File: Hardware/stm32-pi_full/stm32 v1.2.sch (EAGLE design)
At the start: 286 parts, among them IC2 AD8519KS, J1 JUMPER-SMT_2_NC_TRACE_NO-SILK, Q1 PNP, Q2 NPN, Q3 NPN, U1 ESP32-WROOM-32D

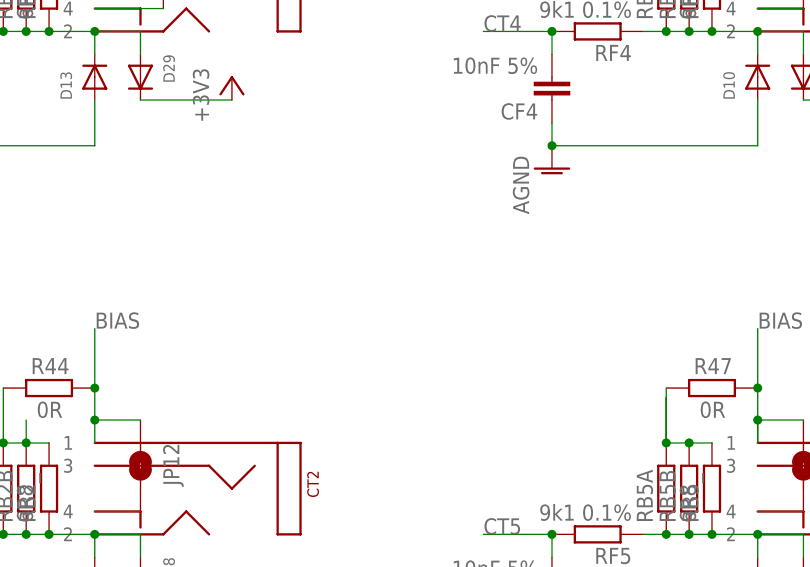
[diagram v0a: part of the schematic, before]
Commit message: pulse detect fix. separated readings timer and posting timer implemented.
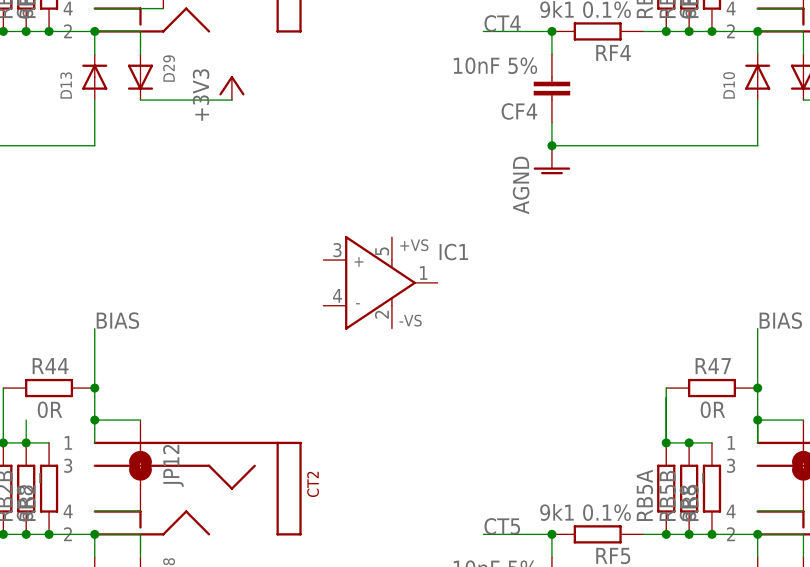
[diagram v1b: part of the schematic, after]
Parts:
- added IC1: AD8519KS, analog-devices:AD8519KS
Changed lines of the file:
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@@
 <part name="C55" library="rcl" library_urn="urn:adsk.eagle:library:334" deviceset="C-EU" device="C0805" package3d_urn="urn:adsk.eagle:package:23617/2" value="47uF"/>
 <part name="TP12" library="SparkFun-Connectors" deviceset="TEST-POINT" device="3"/>
+<part name="IC1" library="analog-devices" library_urn="urn:adsk.eagle:library:102" deviceset="AD8519" device="KS" package3d_urn="urn:adsk.eagle:package:3966/1" value=""/>
 </parts>
 <sheets>
@@
 <attribute name="NAME" x="-2.794" y="68.58" size="1.778" layer="95" font="vector" rot="R90"/>
 </instance>
+<instance part="IC1" gate="P" x="271.78" y="152.4" smashed="yes">
+<attribute name="NAME" x="279.4" y="154.94" size="1.778" layer="95"/>
+<attribute name="VALUE" x="279.4" y="148.59" size="1.778" layer="96"/>
+</instance>
 </instances>

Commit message: modified:   Hardware/stm32-pi_full/stm32 v1.2.brd 	modified:   Hardware/stm32-pi_full/stm32 v1.2.sch 	modified:   Software/Sombrero_VE_Working6/build/Sombrero_VE_Working6.bin
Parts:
- removed C20: 2.2nF, rcl:C-EUC0603
- removed C35, C36: (no value), rcl:C-EUC0603
- removed C50: 1uF, rcl:C-EUC0603
- removed D10, D11, D12, D13, D15, D16, D19, D20, D24, D25, D27, D28, D29, D5, D6, D7, D8, D9: ESD5Z3.3T1G, microbuilder:DIODESOD-523
- removed IC1, IC2: AD8519KS, analog-devices:AD8519KS
- removed JP11, JP13, JP15: JUMPER-SMT_2_NO_NO-SILK_ROUND, SparkFun-Jumpers:JUMPER-SMT_2_NO_NO-SILK_ROUND
- removed R23: 1k, resistor:R-EU_R0603
- removed R38: 39k, resistor:R-EU_R0603
- removed R46, R47, R48: 0R, rcl:R-EU_R0603
- removed R54: 10k, resistor:R-EU_R0603
- removed R6: 0R, resistor:R-EU_R0603
- removed RB1B, RB2B, RB3B, RB4B, RB5B, RB6B, RB7B, RB8B, RB9B: (no value), rcl:R-EU_R0805
- removed TP3, TP5, TP6: TEST-POINTPOGO_PTH, SparkFun-Connectors:TEST-POINTPOGO_PTH
- added LMV1, LMV2, LMV3: LMV824IDG4, LMV824IDG4:LMV824IDG4
- added RB11, RB12, RB13: 510R, rcl:R-EU_R0805
- added RB44, RB55, RB66: 680R, rcl:R-EU_R0805
- added SJ1: JUMPER-SMT_2_NC_TRACE_NO-SILK, SparkFun-Jumpers:JUMPER-SMT_2_NC_TRACE_NO-SILK
- added U2: RFM69HCW/RFM95W, microbuilder:RFM69HCW_SMT
- R55: value 91k -> 10k
- renumbered RB1A to RB1, RB2A to RB2, RB3A to RB3, RB4A to RB4, RB5A to RB5, RB6A to RB6, RB7A to RB7, RB8A to RB8, RB9A to RB9
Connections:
- net CT4 renamed CT4_ADC
- net CT5 renamed CT5_ADC
- net CT6 renamed CT6_ADC
- removed net N$25: R46.2, RB6.2, RB6B.2, RB6_.2
- new net BIAS1: D2.A, D3.C
- new net BIAS456: LMV2.1IN+, LMV2.2IN+, LMV2.3IN+, LMV2.4IN-, LMV2.4OUT, RB44.2, RB55.2, RB66.2
- new net CT4_OUT: LMV2.1OUT, RB11.1, RF4.1
- new net CT5_OUT: LMV2.2OUT, RB12.1, RF5.1
- new net CT6_OUT: LMV2.3OUT, RB13.2, RF6.1
- new net N$12: CT5.3
- new net N$38: CT4.3
- new net N$40: CT6.1, RB6.2, RB66.1, RB6_.2
- net +3V3ANA: now also LMV1.VCC+, LMV2.VCC+, LMV3.VCC+; no longer D15.C, D16.C, D19.C, D20.C, D24.C, D25.C, D27.C, D28.C, D29.C, IC2.+VS
- net AGND: now also LMV1.GND/VCC-, LMV2.GND/VCC-, LMV3.GND/VCC-; no longer C35.2, C36.2, C50.2, D10.A, D11.A, D12.A, D13.A, D5.A, D6.A, D7.A, D8.A, D9.A, IC2.-VS, R54.2
- net BIAS: now also LMV2.4IN+; no longer C35.1, C36.1, CT4.1, CT5.1, CT6.1, D2.A, D3.C, JP11.1, JP13.1, JP15.1, R23.2, R38.1, R46.1, R47.1, R48.1, R6.2, TP3.1
- net CT_IN1: no longer D13.C, D29.A, RB1B.1
- net CT_IN2: no longer D12.C, D28.A, RB2B.1
- net CT_IN3: no longer D11.C, D27.A, RB3B.1
- net CT_IN4: now also LMV2.1IN-, RB11.2; no longer D10.C, D25.A, RB4B.1, RF4.1
- net CT_IN5: now also LMV2.2IN-, RB12.2; no longer D20.A, D9.C, RB5B.1, RF5.1
- net CT_IN6: now also LMV2.3IN-, RB13.1; no longer D24.A, D8.C, RB6B.1, RF6.1
- net CT_IN7: no longer D19.A, D7.C, RB7B.1
- net CT_IN8: no longer D16.A, D6.C, RB8B.1
- net CT_IN9: no longer D15.A, D5.C, RB9B.1
- net N$10: no longer JP13.2
- net N$2: no longer JP11.2
- net N$20: no longer JP15.2
- net N$24: now also CT6.3; no longer R47.2, RB5.2, RB5B.2, RB5_.2
- net N$26: no longer RB1B.2
- net N$27: no longer RB2B.2
- net N$29: no longer RB8B.2
- net N$34: no longer RB9B.2
- net N$35: now also CT4.1, RB44.1; no longer R48.2, RB4B.2
- net N$36: no longer RB7B.2
- net N$37: no longer RB3B.2
- net N$7: now also CT5.1, RB5.2, RB55.1, RB5_.2; no longer C50.1, R23.1
- net OPAMP_INVERT-: now also SJ1.1; no longer C20.1, IC2.IN-, R38.2, R54.1, TP6.1
- net OPAMP_NON-INVERT+: no longer IC2.IN+, TP2.1
- net OPAMP_OUT: now also SJ1.2, TP2.1; no longer C20.2, IC2.OUT, R6.1, TP5.1
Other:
- note added: "RFMxx"
- note removed: "RFM69"
- moved on the sheet: CF4, CF5, CF6, CV1, CV2, CV3, CV4, D1, D2, D3, D4, LMV824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

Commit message: update
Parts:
- RB1, RB2, RB3, RB4, RB5, RB6, RB7, RB8, RB9: value 6R8 -> 6R81
- RB11, RB12, RB13: value 510R -> 510R 0.1%
- RB44, RB55, RB66: value 680R -> 680R | 681R 0.1%
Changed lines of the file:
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@@
 <drawing>
 <settings>
-<setting alwaysvectorfont="no"/>
+<setting alwaysvectorfont="yes"/>
 <setting keepoldvectorfont="yes"/>
 <setting verticaltext="up"/>
@@
 <part name="TP20" library="SparkFun-Connectors" deviceset="TEST-POINT" device="POGO_PTH" value="TEST-POINTPOGO_PTH"/>
 <part name="HSE" library="6mm 3m5mm crystal multicomp pro abracon" deviceset="6MM_3.5MM_CRYSTAL" device=""/>
-<part name="RB1" library="rcl" library_urn="urn:adsk.eagle:library:334" deviceset="R-EU_" device="R0805" package3d_urn="urn:adsk.eagle:package:23553/2" value="6R8"/>
-<part name="RB4" library="rcl" library_urn="urn:adsk.eagle:library:334" deviceset="R-EU_" device="R0805" package3d_urn="urn:adsk.eagle:package:23553/2" value="6R8"/>
-<part name="RB7" library="rcl" library_urn="urn:adsk.eagle:library:334" deviceset="R-EU_" device="R0805" package3d_urn="urn:adsk.eagle:package:23553/2" value="6R8"/>
-<part name="RB8" library="rcl" library_urn="urn:adsk.eagle:library:334" deviceset="R-EU_" device="R0805" package3d_urn="urn:adsk.eagle:package:23553/2" value="6R8"/>
-<part name="RB5" library="rcl" library_urn="urn:adsk.eagle:library:334" deviceset="R-EU_" device="R0805" package3d_urn="urn:adsk.eagle:package:23553/2" value="6R8"/>
-<part name="RB9" library="rcl" library_urn="urn:adsk.eagle:library:334" deviceset="R-EU_" device="R0805" package3d_urn="urn:adsk.eagle:package:23553/2" value="6R8"/>
-<part name="RB6" library="rcl" library_urn="urn:adsk.eagle:library:334" deviceset="R-EU_" device="R0805" package3d_urn="urn:adsk.eagle:package:23553/2" value="6R8"/>
-<part name="RB2" library="rcl" library_urn="urn:adsk.eagle:library:334" deviceset="R-EU_" device="R0805" package3d_urn="urn:adsk.eagle:package:23553/2" value="6R8"/>
-<part name="RB3" library="rcl" library_urn="urn:adsk.eagle:library:334" deviceset="R-EU_" device="R0805" package3d_urn="urn:adsk.eagle:package:23553/2" value="6R8"/>
+<part name="RB1" library="rcl" library_urn="urn:adsk.eagle:library:334" deviceset="R-EU_" device="R0805" package3d_urn="urn:adsk.eagle:package:23553/2" value="6R81"/>
+<part name="RB4" library="rcl" library_urn="urn:adsk.eagle:library:334" deviceset="R-EU_" device="R0805" package3d_urn="urn:adsk.eagle:package:23553/2" value="6R81"/>
+<part name="RB7" library="rcl" library_urn="urn:adsk.eagle:library:334" deviceset="R-EU_" device="R0805" package3d_urn="urn:adsk.eagle:package:23553/2" value="6R81"/>
+<part name="RB8" library="rcl" library_urn="urn:adsk.eagle:library:334" deviceset="R-EU_" device="R0805" package3d_urn="urn:adsk.eagle:package:23553/2" value="6R81"/>
+<part name="RB5" library="rcl" library_urn="urn:adsk.eagle:library:334" deviceset="R-EU_" device="R0805" package3d_urn="urn:adsk.eagle:package:23553/2" value="6R81"/>
+<part name="RB9" library="rcl" library_urn="urn:adsk.eagle:library:334" deviceset="R-EU_" device="R0805" package3d_urn="urn:adsk.eagle:package:23553/2" value="6R81"/>
+<part name="RB6" library="rcl" library_urn="urn:adsk.eagle:library:334" deviceset="R-EU_" device="R0805" package3d_urn="urn:adsk.eagle:package:23553/2" value="6R81"/>
+<part name="RB2" library="rcl" library_urn="urn:adsk.eagle:library:334" deviceset="R-EU_" device="R0805" package3d_urn="urn:adsk.eagle:package:23553/2" value="6R81"/>
+<part name="RB3" library="rcl" library_urn="urn:adsk.eagle:library:334" deviceset="R-EU_" device="R0805" package3d_urn="urn:adsk.eagle:package:23553/2" value="6R81"/>
 <part name="R33" library="rcl" library_urn="urn:adsk.eagle:library:334" deviceset="R-EU_" device="R0603" package3d_urn="urn:adsk.eagle:package:23555/3" value="10k"/>
 <part name="+3V19" library="supply1" library_urn="urn:adsk.eagle:library:371" deviceset="+3V3" device=""/>
@@
 <attribute name="MPN" value="MBR130LSFT1G"/>
 </part>
-<part name="RB55" library="rcl" library_urn="urn:adsk.eagle:library:334" deviceset="R-EU_" device="R0805" package3d_urn="urn:adsk.eagle:package:23553/2" value="680R"/>
+<part name="RB55" library="rcl" library_urn="urn:adsk.eagle:library:334" deviceset="R-EU_" device="R0805" package3d_urn="urn:adsk.eagle:package:23553/2" value="680R | 681R 0.1%"/>
 <part name="U2" library="microbuilder" deviceset="RFM69HCW" device="_SMT" value="RFM69HCW/RFM95W"/>
-<part name="RB11" library="rcl" library_urn="urn:adsk.eagle:library:334" deviceset="R-EU_" device="R0805" package3d_urn="urn:adsk.eagle:package:23553/2" value="510R"/>
-<part name="RB44" library="rcl" library_urn="urn:adsk.eagle:library:334" deviceset="R-EU_" device="R0805" package3d_urn="urn:adsk.eagle:package:23553/2" value="680R"/>
-<part name="RB66" library="rcl" library_urn="urn:adsk.eagle:library:334" deviceset="R-EU_" device="R0805" package3d_urn="urn:adsk.eagle:package:23553/2" value="680R"/>
+<part name="RB11" library="rcl" library_urn="urn:adsk.eagle:library:334" deviceset="R-EU_" device="R0805" package3d_urn="urn:adsk.eagle:package:23553/2" value="510R 0.1%"/>
+<part name="RB44" library="rcl" library_urn="urn:adsk.eagle:library:334" deviceset="R-EU_" device="R0805" package3d_urn="urn:adsk.eagle:package:23553/2" value="680R | 681R 0.1%"/>
+<part name="RB66" library="rcl" library_urn="urn:adsk.eagle:library:334" deviceset="R-EU_" device="R0805" package3d_urn="urn:adsk.eagle:package:23553/2" value="680R | 681R 0.1%"/>
 <part name="LMV1" library="LMV824IDG4" deviceset="LMV824IDG4" device=""/>
 <part name="LMV2" library="LMV824IDG4" deviceset="LMV824IDG4" device=""/>
 <part name="LMV3" library="LMV824IDG4" deviceset="LMV824IDG4" device=""/>
-<part name="RB12" library="rcl" library_urn="urn:adsk.eagle:library:334" deviceset="R-EU_" device="R0805" package3d_urn="urn:adsk.eagle:package:23553/2" value="510R"/>
-<part name="RB13" library="rcl" library_urn="urn:adsk.eagle:library:334" deviceset="R-EU_" device="R0805" package3d_urn="urn:adsk.eagle:package:23553/2" value="510R"/>
+<part name="RB12" library="rcl" library_urn="urn:adsk.eagle:library:334" deviceset="R-EU_" device="R0805" package3d_urn="urn:adsk.eagle:package:23553/2" value="510R 0.1%"/>
+<part name="RB13" library="rcl" library_urn="urn:adsk.eagle:library:334" deviceset="R-EU_" device="R0805" package3d_urn="urn:adsk.eagle:package:23553/2" value="510R 0.1%"/>
 </parts>
 <sheets>

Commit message: brd changes
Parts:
- removed JP10, JP12, JP14, JP16, JP17, JP18: JUMPER-SMT_2_NO_NO-SILK_ROUND, SparkFun-Jumpers:JUMPER-SMT_2_NO_NO-SILK_ROUND
- removed R42, R44, R45, R49, R50, R51: 0R, rcl:R-EU_R0603
- added RB10, RB14, RB15, RB16, RB17, RB18: 510R 0.1%, rcl:R-EU_R0805
- added RB19, RB20, RB21, RB22, RB23, RB24: 680R | 681R 0.1%, rcl:R-EU_R0805
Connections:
- net CT1 renamed CT1_ADC
- net CT2 renamed CT2_ADC
- net CT3 renamed CT3_ADC
- removed net N$29: R50.2, RB8.2, RB8_.2
- removed net N$34: R51.2, RB9.2, RB9_.2
- removed net N$37: R45.2, RB3.2, RB3_.2
- new net BIAS123: LMV1.1IN+, LMV1.2IN+, LMV1.3IN+, LMV1.4IN-, LMV1.4OUT, RB19.2, RB20.2, RB21.2
- new net BIAS789: LMV3.1IN+, LMV3.2IN+, LMV3.3IN+, LMV3.4IN-, LMV3.4OUT, RB22.2, RB23.2, RB24.2
- new net CT1_OUT: LMV1.1OUT, RB10.1, RF1.1
- new net CT2_OUT: LMV1.2OUT, RB14.1, RF2.1
- new net CT3_OUT: LMV1.3OUT, RB15.2, RF3.1
- new net CT7_OUT: LMV3.1OUT, RB16.1, RF7.1
- new net CT8_OUT: LMV3.2OUT, RB17.1, RF8.1
- new net CT9_OUT: LMV3.3OUT, RB18.2, RF9.1
- new net N$43: CT9.1, RB24.1, RB9.2, RB9_.2
- new net N$45: CT8.1, RB23.1, RB8.2, RB8_.2
- new net N$46: CT7.1, RB22.1, RB7.2, RB7_.2
- net BIAS: now also LMV1.4IN+, LMV3.4IN+; no longer CT1.1, CT2.1, CT3.1, CT7.1, CT8.1, CT9.1, JP10.1, JP12.1, JP14.1, JP16.1, JP17.1, JP18.1, R42.1, R44.1, R45.1, R49.1, R50.1, R51.1
- net CT_IN1: now also LMV1.1IN-, RB10.2; no longer RF1.1
- net CT_IN2: now also LMV1.2IN-, RB14.2; no longer RF2.1
- net CT_IN3: now also LMV1.3IN-, RB15.1; no longer RF3.1
- net CT_IN7: now also LMV3.1IN-, RB16.2; no longer RF7.1
- net CT_IN8: now also LMV3.2IN-, RB17.2; no longer RF8.1
- net CT_IN9: now also LMV3.3IN-, RB18.1; no longer RF9.1
- net N$1: no longer JP10.2
- net N$13: no longer JP14.2
- net N$21: no longer JP16.2
- net N$22: no longer JP17.2
- net N$23: no longer JP18.2
- net N$26: now also CT1.1, RB19.1; no longer R42.2
- net N$27: now also CT2.1, RB20.1; no longer R44.2
- net N$36: now also CT3.1, RB21.1, RB3.2, RB3_.2; no longer R49.2, RB7.2, RB7_.2
- net N$8: no longer JP12.2
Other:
- moved on the sheet: CF1, CF2, CF3, CF7, CF8, CF9, LMV1, LMV2, LMV3, RB11, RB12, RB13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

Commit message: update
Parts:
- removed C53: 22uF, rcl:C-EUC0805
- added C20, C35: 22uF, rcl:C-EUC0805
- added FB10, FB11, FB6: (no value), microbuilder:FERRITE_0603
- added IC1: TS461CLT, TS461CLT:TS461CLT
- added JP3, JP5: JUMPER-SMT_3_1-NC_TRACE_NO-SILK, SparkFun-Jumpers:JUMPER-SMT_3_1-NC_TRACE_NO-SILK
- added JP6: JUMPER-SMT_2_NC_PASTE_SILK, SparkFun-Jumpers:JUMPER-SMT_2_NC_PASTE_SILK
- added R6: 20R, rcl:R-EU_R0603
- added TP3, TP5, TP6: TEST-POINTPOGO_PTH, SparkFun-Connectors:TEST-POINTPOGO_PTH
- C11, C23: value 1uF -> 22uf
- FB1: value (none) -> 1600R
- FB2: value (none) -> 0R
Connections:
- removed net BIAS1: D2.A, D3.C
- removed net OPAMP_NON-INVERT+: C53.1, R55.1, R56.2, STM32F303VE.PD11
- new net ANT_LORA: JP6.1, U2.ANT
- new net BIAS_SOT23: IC1.-V, IC1.OUT, JP5.2
- new net DIO1_RFM: STM32F303VE.PE4, U2.DIO1
- new net N$25: FB10.P$1, MCP1825.+3V3
- new net N$29: C11.1, C37.1, FB6.P$1, REF19X.!SHDN, REF19X.VIN, TP11.1
- new net N$34: FB11.P$1, MCP1825(ANALOG).+3V3
- new net N$37: JP3.2, R55.1, R56.2
- new net N$39: C20.1, IC1.+V, JP3.3, TP6.1
- new net N$42: JP5.3, R6.1, TP3.1
- new net STM32_OPAMP_NON-INVERT+: C35.1, JP3.1, STM32F303VE.PD11
- new net STM32_OPAMP_OUT: JP5.1, STM32F303VE.PB12, TP2.1
- net +3V3: now also FB10.P$2; no longer MCP1825.+3V3
- net +3V3ANA: now also FB11.P$2, FB6.P$2, IC1.VDD; no longer C11.1, C37.1, MCP1825(ANALOG).+3V3, REF19X.!SHDN, REF19X.VIN, TP11.1
- net AGND: now also C20.2, C35.2, IC1.VCC; no longer C53.2
- net ANT: now also JP6.2
- net BIAS: now also D2.A, D3.C, R6.2, TP5.1
- net DGND: now also U2.GND@2
- net DIO0_RFM: now also U2.DIO0
- net OPAMP_OUT: no longer STM32F303VE.PB12, TP2.1
- net RGND: now also U2.GND@1, U2.GND@3
- net RST_RFM: now also U2.RESET
- net SPI4_CLK_MASTER: now also U2.SCK
- net SPI4_CS_RFM69_MASTER: now also U2.NSS
- net SPI4_MISO_MASTER: now also U2.MISO
- net SPI4_MOSI_MASTER: now also U2.MOSI
- net VDD: now also U2.VDD
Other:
- note added: "maybe DNGA comes off the ANA supply with FB in series"
- note removed: "maybe DNGA comes off the ana supply with FB in series"
- moved on the sheet: C33, C43, D2, D3, R55, TP1
